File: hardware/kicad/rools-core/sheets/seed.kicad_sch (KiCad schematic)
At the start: 1 part

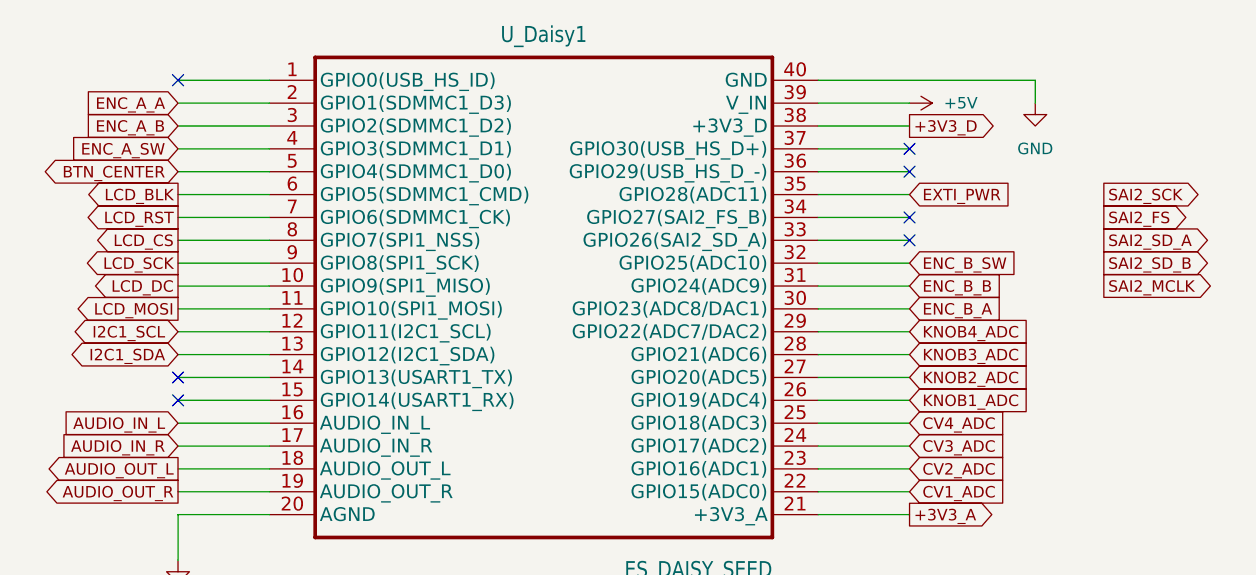
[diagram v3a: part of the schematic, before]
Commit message: Sync Core schematic Rev 0.2 with docs and firmware.
Align DAC8565/OPA4171 CV path (2.5V internal ref, 12.5k/100k), LM393 power-fail hold-up, and SPI1 CV driver fixes (LDAC polarity, debounced save with backlight off).

Co-authored-by: Cursor <cursoragent@cursor.com>
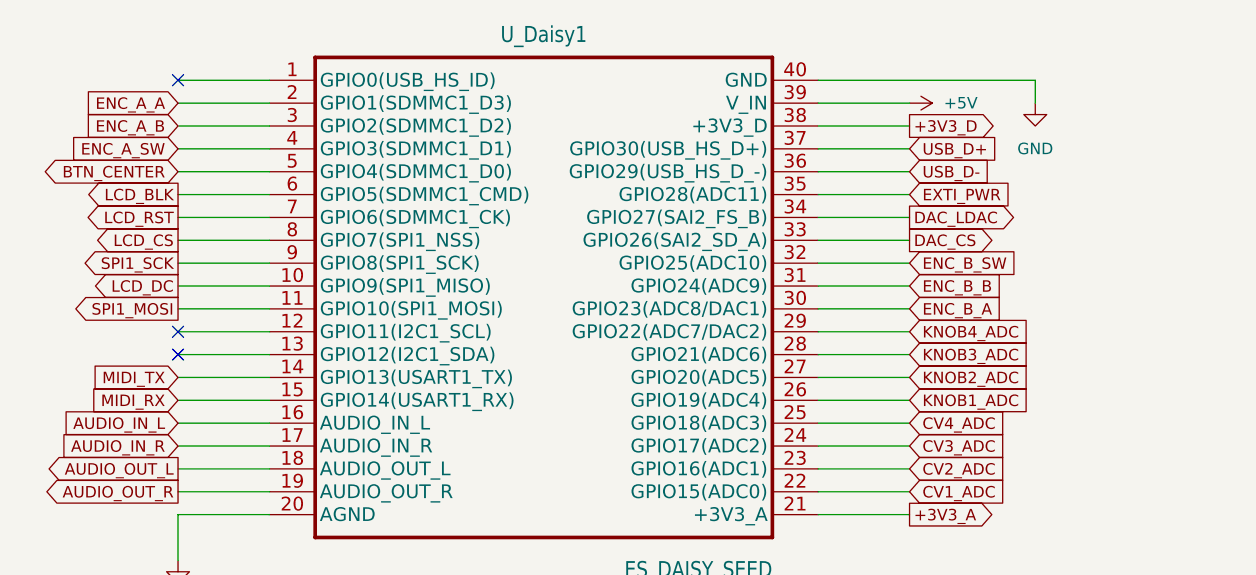
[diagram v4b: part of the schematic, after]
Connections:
- net MIDI_TX: now reaches U_Daisy1.14 (GPIO13(USART1_TX))
- net MIDI_RX: now reaches U_Daisy1.15 (GPIO14(USART1_RX))
- net DAC_CS: now reaches U_Daisy1.33 (GPIO26(SAI2_SD_A))
- net DAC_LDAC: now reaches U_Daisy1.34 (GPIO27(SAI2_FS_B))
- net USB_D-: now reaches U_Daisy1.36 (GPIO29(USB_HS_D_-))
- net USB_D+: now reaches U_Daisy1.37 (GPIO30(USB_HS_D+))
- net I2C1_SCL: no longer names the net of U_Daisy1.12 (GPIO11(I2C1_SCL))
- net I2C1_SDA: no longer names the net of U_Daisy1.13 (GPIO12(I2C1_SDA))
- net LCD_MOSI renamed SPI1_MOSI
- net LCD_SCK renamed SPI1_SCK
- no-connect marks 7 -> 3
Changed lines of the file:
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@@
 	)
 	(no_connect
-		(at 172.72 83.82)
+		(at 91.44 101.6)
 	)
 	(no_connect
-		(at 172.72 91.44)
+		(at 91.44 104.14)
 	)
 	(no_connect
 		(at 91.44 73.66)
 	)
-	(no_connect
-		(at 91.44 106.68)
-	)
-	(no_connect
-		(at 172.72 81.28)
-	)
-	(no_connect
-		(at 91.44 109.22)
-	)
-	(no_connect
-		(at 172.72 88.9)
-	)
 	(wire
 		(pts
@@
 	(wire
 		(pts
-			(xy 101.6 93.98) (xy 91.44 93.98)
+			(xy 91.44 93.98) (xy 101.6 93.98)
 		)
 		(stroke
@@
 		)
 	)
-	(global_label "LCD_MOSI"
+	(global_label "SPI1_MOSI"
 		(shape output)
 		(at 91.44 99.06 180)
@@
 		(property "Intersheetrefs" "${INTERSHEET_REFS}"
 			(at 91.44 99.06 0)
-			(hide yes)
-			(show_name no)
-			(do_not_autoplace no)
-			(effects
-				(font
-					(size 1.27 1.27)
-				)
-			)
-		)
-	)
-	(global_label "SAI2_SCK"
-		(shape output)
-		(at 194.31 86.36 0)
-		(effects
-			(font
-				(size 1.27 1.27)
-			)
-			(justify left)
-		)
-		(property "Intersheetrefs" "${INTERSHEET_REFS}"
-			(at 194.31 86.36 0)
 			(hide yes)
 			(show_name no)
@@
 		)
 	)
-	(global_label "LCD_SCK"
+	(global_label "MIDI_TX"
+		(shape input)
+		(at 91.44 106.68 180)
+		(fields_autoplaced yes)
+		(effects
+			(font
+				(size 1.27 1.27)
+			)
+			(justify right)
+		)
+		(property "Intersheetrefs" "${INTERSHEET_REFS}"
+			(at 81.284 106.68 0)
+			(hide yes)
+			(show_name no)
+			(do_not_autoplace no)
+			(effects
+				(font
+					(size 1.27 1.27)
+				)
+				(justify right)
+			)
+		)
+	)
+	(global_label "SPI1_SCK"
 		(shape output)
 		(at 91.44 93.98 180)
@@
 		)
 	)
-	(global_label "I2C1_SDA"
-		(shape bidirectional)
-		(at 91.44 104.14 180)
-		(effects
-			(font
-				(size 1.27 1.27)
-			)
-			(justify right)
-		)
-		(property "Intersheetrefs" "${INTERSHEET_REFS}"
-			(at 91.44 104.14 0)
-			(hide yes)
-			(show_name no)
-			(do_not_autoplace no)
-			(effects
-				(font
-					(size 1.27 1.27)
-				)
-			)
-		)
-	)
-	(global_label "I2C1_SCL"
-		(shape bidirectional)
-		(at 91.44 101.6 180)
-		(effects
-			(font
-				(size 1.27 1.27)
-			)
-			(justify right)
-		)
-		(property "Intersheetrefs" "${INTERSHEET_REFS}"
-			(at 91.44 101.6 0)
-			(hide yes)
-			(show_name no)
-			(do_not_autoplace no)
-			(effects
-				(font
-					(size 1.27 1.27)
-				)
+	(global_label "MIDI_RX"
+		(shape input)
+		(at 91.44 109.22 180)
+		(fields_autoplaced yes)
+		(effects
+			(font
+				(size 1.27 1.27)
+			)
+			(justify right)
+		)
+		(property "Intersheetrefs" "${INTERSHEET_REFS}"
+			(at 80.9816 109.22 0)
+			(hide yes)
+			(show_name no)
+			(do_not_autoplace no)
+			(effects
+				(font
+					(size 1.27 1.27)
+				)
+				(justify right)
 			)
 		)
@@
 				)
 				(justify left)
-			)
-		)
-	)
-	(global_label "SAI2_FS"
-		(shape output)
-		(at 194.31 88.9 0)
-		(effects
-			(font
-				(size 1.27 1.27)
-			)
-			(justify left)
-		)
-		(property "Intersheetrefs" "${INTERSHEET_REFS}"
-			(at 194.31 88.9 0)
-			(hide yes)
-			(show_name no)
-			(do_not_autoplace no)
-			(effects
-				(font
-					(size 1.27 1.27)
-				)
 			)
 		)
@@
 		)
 	)
+	(global_label "USB_D-"
+		(shape input)
+		(at 172.72 83.82 0)
+		(fields_autoplaced yes)
+		(effects
+			(font
+				(size 1.27 1.27)
+			)
+			(justify left)
+		)
+		(property "Intersheetrefs" "${INTERSHEET_REFS}"
+			(at 183.4203 83.82 0)
+			(hide yes)
+			(show_name no)
+			(do_not_autoplace no)
+			(effects
+				(font
+					(size 1.27 1.27)
+				)
+				(justify left)
+			)
+		)
+	)
 	(global_label "KNOB4_ADC"
 		(shape input)
@@
 		)
 	)
-	(global_label "SAI2_SD_A"
-		(shape output)
-		(at 194.31 91.44 0)
-		(effects
-			(font
-				(size 1.27 1.27)
-			)
-			(justify left)
-		)
-		(property "Intersheetrefs" "${INTERSHEET_REFS}"
-			(at 194.31 91.44 0)
-			(hide yes)
-			(show_name no)
-			(do_not_autoplace no)
-			(effects
-				(font
-					(size 1.27 1.27)
-				)
-			)
-		)
-	)
 	(global_label "ENC_B_A"
 		(shape input)
@@
 		)
 	)
+	(global_label "USB_D+"
+		(shape input)
+		(at 172.72 81.28 0)
+		(fields_autoplaced yes)
+		(effects
+			(font
+				(size 1.27 1.27)
+			)
+			(justify left)
+		)
+		(property "Intersheetrefs" "${INTERSHEET_REFS}"
+			(at 183.4203 81.28 0)
+			(hide yes)
+			(show_name no)
+			(do_not_autoplace no)
+			(effects
+				(font
+					(size 1.27 1.27)
+				)
+				(justify left)
+			)
+		)
+	)
 	(global_label "KNOB1_ADC"
 		(shape input)
@@
 		)
 	)
+	(global_label "DAC_CS"
+		(shape output)
+		(at 172.72 91.44 0)
+		(fields_autoplaced yes)
+		(effects
+			(font
+				(size 1.27 1.27)
+			)
+			(justify left)
+		)
+		(property "Intersheetrefs" "${INTERSHEET_REFS}"
+			(at 182.876 91.44 0)
+			(hide yes)
+			(show_name no)
+			(do_not_autoplace no)
+			(effects
+				(font
+					(size 1.27 1.27)
+				)
+				(justify left)
+			)
+		)
+	)
 	(global_label "AUDIO_IN_L"
 		(shape input)
@@
 		)
 	)
-	(global_label "SAI2_MCLK"
+	(global_label "DAC_LDAC"
 		(shape output)
-		(at 194.31 96.52 0)
-		(effects
-			(font
-				(size 1.27 1.27)
-			)
-			(justify left)
-		)
-		(property "Intersheetrefs" "${INTERSHEET_REFS}"
-			(at 194.31 96.52 0)
-			(hide yes)
-			(show_name no)
-			(do_not_autoplace no)
-			(effects
-				(font
-					(size 1.27 1.27)
-				)
-			)
-		)
-	)
-	(global_label "SAI2_SD_B"
-		(shape output)
-		(at 194.31 93.98 0)
-		(effects
-			(font
-				(size 1.27 1.27)
-			)
-			(justify left)
-		)
-		(property "Intersheetrefs" "${INTERSHEET_REFS}"
-			(at 194.31 93.98 0)
-			(hide yes)
-			(show_name no)
-			(do_not_autoplace no)
-			(effects
-				(font
-					(size 1.27 1.27)
-				)
-			)
-		)
+		(at 172.72 88.9 0)
+		(fields_autoplaced yes)
+		(effects
+			(font
+				(size 1.27 1.27)
+			)
+			(justify left)
+		)
+		(property "Intersheetrefs" "${INTERSHEET_REFS}"
+			(at 185.0532 88.9 0)
+			(hide yes)
+			(show_name no)
+			(do_not_autoplace no)
+			(effects
+				(font
+					(size 1.27 1.27)
+				)
+				(justify left)
+			)
+		)

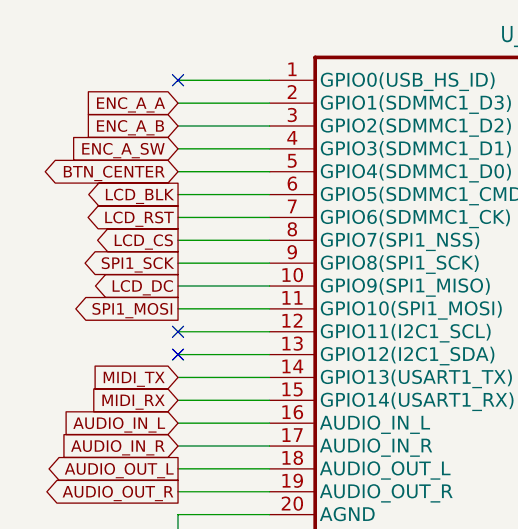
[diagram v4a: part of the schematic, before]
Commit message: Finalize Core schematic pin map and JLC BOM for assembly.
MIDI USART1 on D13/D14, DAC8565 on D26/D27, and document P2 EXP_BUS so Exp I/O no longer conflicts with CV Out.

Co-authored-by: Cursor <cursoragent@cursor.com>
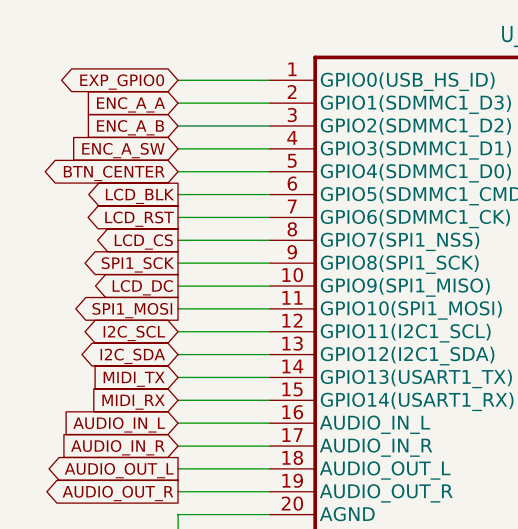
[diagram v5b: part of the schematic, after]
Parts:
- U_Daisy1: footprint ES_Daisy_Patch_Rev8:ES_DAISY_SEED -> Module:Electrosmith_Daisy_Seed
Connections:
- net EXP_GPIO0: now reaches U_Daisy1.1 (GPIO0(USB_HS_ID))
- net I2C_SCL: now reaches U_Daisy1.12 (GPIO11(I2C1_SCL))
- net I2C_SDA: now reaches U_Daisy1.13 (GPIO12(I2C1_SDA))
- no-connect marks 3 -> 0
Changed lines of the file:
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@@
 		(comment 1 "STM32H7 — 贴片/沉板 USB 见 ADR-013")
-	)
-	(no_connect
-		(at 91.44 101.6)
-	)
-	(no_connect
-		(at 91.44 104.14)
-	)
-	(no_connect
-		(at 91.44 73.66)
 	)
 	(wire
@@
 		)
 	)
+	(global_label "EXP_GPIO0"
+		(shape bidirectional)
+		(at 91.44 73.66 180)
+		(fields_autoplaced yes)
+		(effects
+			(font
+				(size 1.27 1.27)
+			)
+			(justify right)
+		)
+		(property "Intersheetrefs" "${INTERSHEET_REFS}"
+			(at 77.0628 73.66 0)
+			(hide yes)
+			(show_name no)
+			(do_not_autoplace no)
+			(effects
+				(font
+					(size 1.27 1.27)
+				)
+				(justify right)
+			)
+		)
+	)
 	(global_label "ENC_A_A"
 		(shape input)
@@
 		)
 	)
+	(global_label "I2C_SCL"
+		(shape bidirectional)
+		(at 91.44 101.6 180)
+		(fields_autoplaced yes)
+		(effects
+			(font
+				(size 1.27 1.27)
+			)
+			(justify right)
+		)
+		(property "Intersheetrefs" "${INTERSHEET_REFS}"
+			(at 79.7842 101.6 0)
+			(hide yes)
+			(show_name no)
+			(do_not_autoplace no)
+			(effects
+				(font
+					(size 1.27 1.27)
+				)
+				(justify right)
+			)
+		)
+	)
 	(global_label "LCD_DC"
 		(shape output)
@@
 					(size 1.27 1.27)
 				)
+			)
+		)
+	)
+	(global_label "I2C_SDA"
+		(shape bidirectional)
+		(at 91.44 104.14 180)
+		(fields_autoplaced yes)
+		(effects
+			(font
+				(size 1.27 1.27)
+			)
+			(justify right)
+		)
+		(property "Intersheetrefs" "${INTERSHEET_REFS}"
+			(at 79.7237 104.14 0)
+			(hide yes)
+			(show_name no)
+			(do_not_autoplace no)
+			(effects
+				(font
+					(size 1.27 1.27)
+				)
+				(justify right)
 			)
 		)
@@
 			)
 		)
-		(property "Footprint" "ES_Daisy_Patch_Rev8:ES_DAISY_SEED"
+		(property "Footprint" "Module:Electrosmith_Daisy_Seed"
 			(at 132.08 96.52 0)
 			(hide yes)
@@
 		(property "Description" ""
 			(at 127.508 128.27 0)
+			(hide yes)
+			(show_name no)
+			(do_not_autoplace no)
+			(effects
+				(font
+					(size 1.27 1.27)
+				)
+			)
+		)
+		(property "LCSC" ""
+			(at 132.08 96.52 0)
 			(hide yes)
 			(show_name no)
@@
 					(reference "U_Daisy1")
 					(unit 1)
-				)
-			)
+					(variant
+						(name "LCSC")
+					)
+				)
+			)

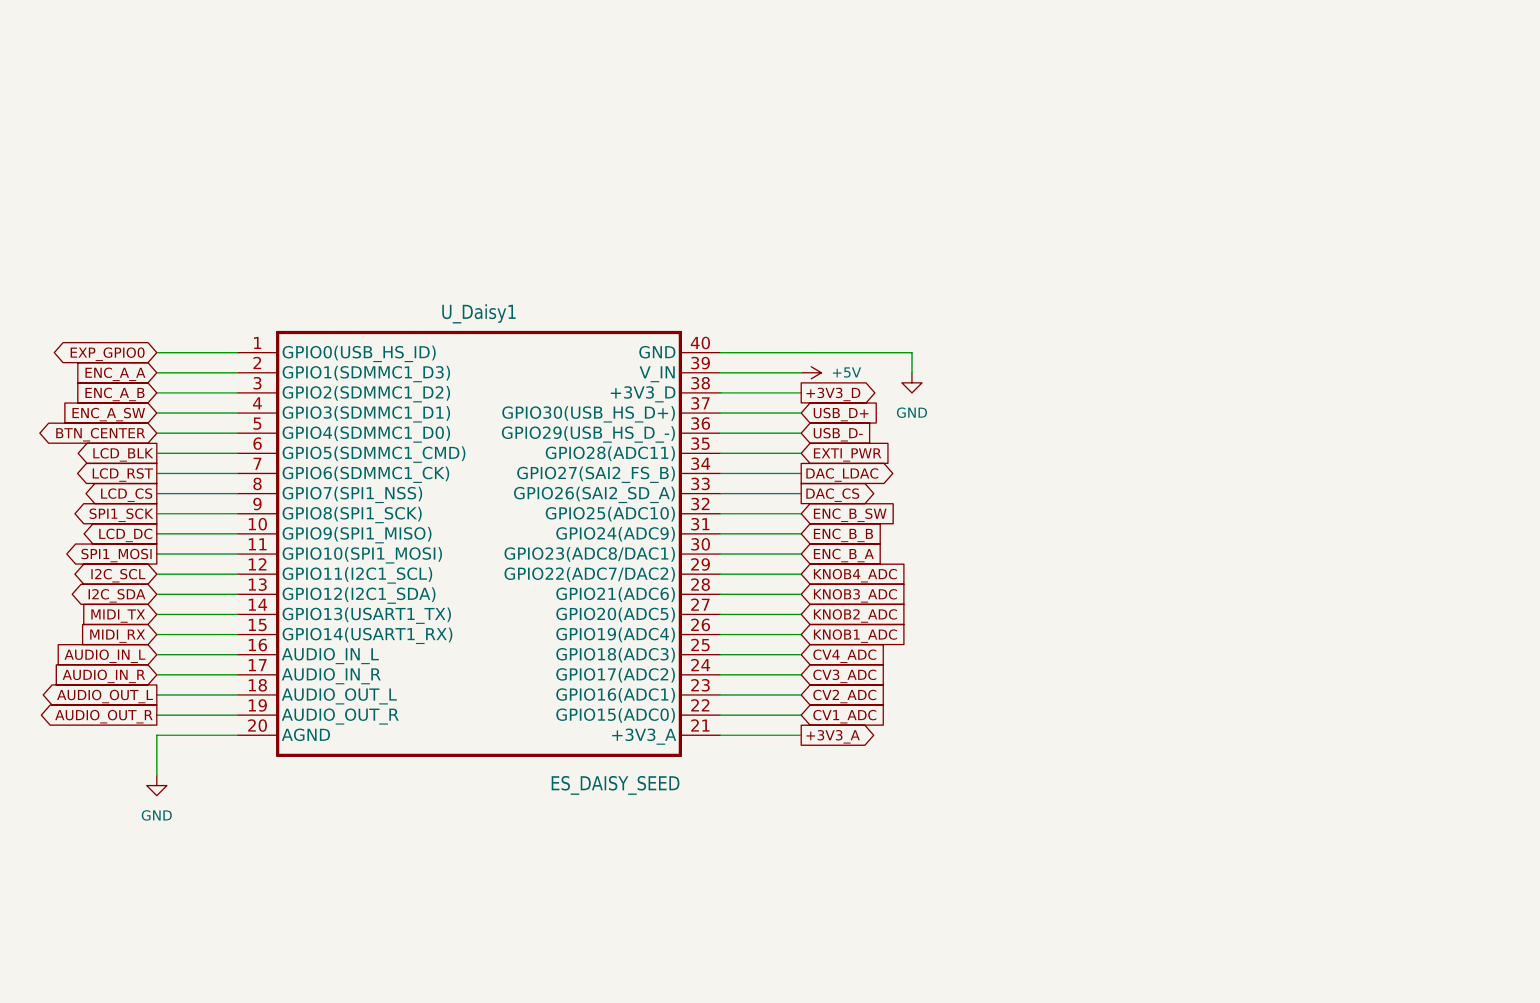
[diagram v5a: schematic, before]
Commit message: Route Core PCB and place Daisy Seed on the daughterboard.
Sync schematic sheets with the split-board layout and updated interconnects.

Co-authored-by: Cursor <cursoragent@cursor.com>
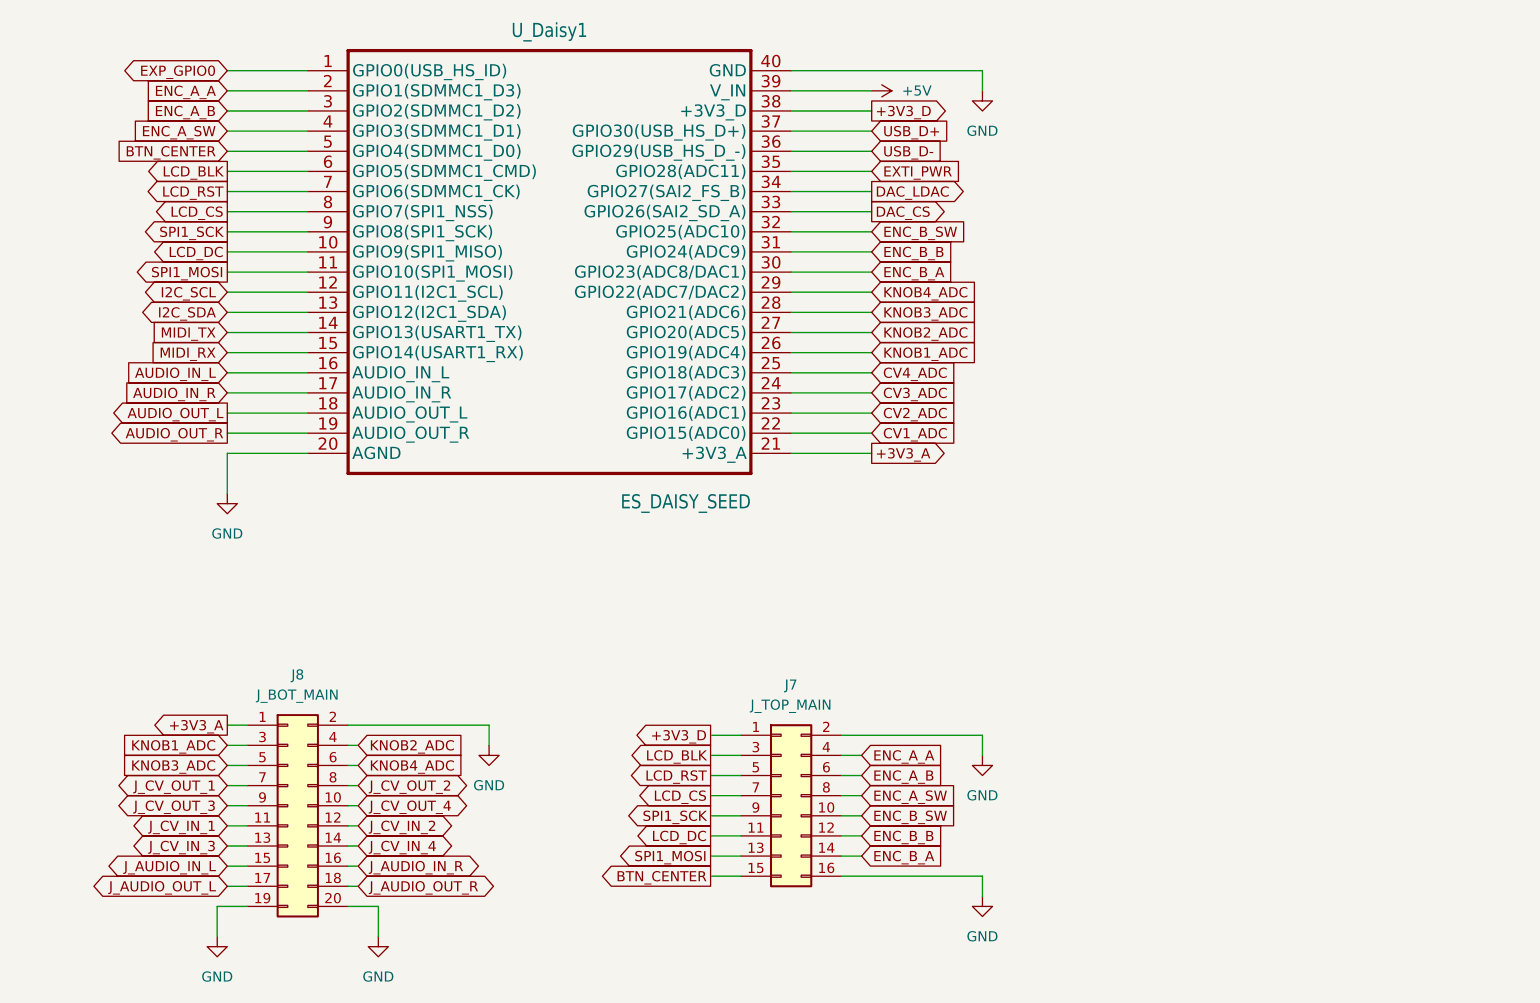
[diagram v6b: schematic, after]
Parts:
- added J7: J_TOP_MAIN, Connector_PinSocket_2.54mm:PinSocket_2x08_P2.54mm_Vertical_SMD, symbol Connector_Generic:Conn_02x08_Odd_Even
- added J8: J_BOT_MAIN, Connector_PinSocket_2.54mm:PinSocket_2x10_P2.54mm_Vertical_SMD, symbol Connector_Generic:Conn_02x10_Odd_Even
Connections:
- net +3V3_A: now also J8.1 (Pin_1)
- net +3V3_D: now also J7.1 (Pin_1)
- net BTN_CENTER: now also J7.15 (Pin_15)
- net ENC_A_A: now also J7.4 (Pin_4)
- net ENC_A_B: now also J7.6 (Pin_6)
- net ENC_A_SW: now also J7.8 (Pin_8)
- net ENC_B_A: now also J7.14 (Pin_14)
- net ENC_B_B: now also J7.12 (Pin_12)
- net ENC_B_SW: now also J7.10 (Pin_10)
- net GND: now also J7.16 (Pin_16), J7.2 (Pin_2), J8.19 (Pin_19), J8.2 (Pin_2), J8.20 (Pin_20)
- net KNOB1_ADC: now also J8.3 (Pin_3)
- net KNOB2_ADC: now also J8.4 (Pin_4)
- net KNOB3_ADC: now also J8.5 (Pin_5)
- net KNOB4_ADC: now also J8.6 (Pin_6)
- net LCD_BLK: now also J7.3 (Pin_3)
- net LCD_CS: now also J7.7 (Pin_7)
- net LCD_DC: now also J7.11 (Pin_11)
- net LCD_RST: now also J7.5 (Pin_5)
- net SPI1_MOSI: now also J7.13 (Pin_13)
- net SPI1_SCK: now also J7.9 (Pin_9)
- new net J_AUDIO_IN_L: J8.15 (Pin_15)
- new net J_AUDIO_IN_R: J8.16 (Pin_16)
- new net J_AUDIO_OUT_L: J8.17 (Pin_17)
- new net J_AUDIO_OUT_R: J8.18 (Pin_18)
- new net J_CV_IN_1: J8.11 (Pin_11)
- new net J_CV_IN_2: J8.12 (Pin_12)
- new net J_CV_IN_3: J8.13 (Pin_13)
- new net J_CV_IN_4: J8.14 (Pin_14)
- new net J_CV_OUT_1: J8.7 (Pin_7)
- new net J_CV_OUT_2: J8.8 (Pin_8)
- new net J_CV_OUT_3: J8.9 (Pin_9)
- new net J_CV_OUT_4: J8.10 (Pin_10)
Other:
- moved on the sheet: U_Daisy1
